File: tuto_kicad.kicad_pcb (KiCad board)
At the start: 4 copper layers, 48 x 38 mm, 46 parts, among them J201 Conn_ST_STDC14, J202 GPIO, J301 USB_C_Receptacle_USB2.0_16P, U201 STM32G431KBT6, U202 ADXL343, U301 MIC5317-3.3YM5-TR, U302 USBLC6-2SC6, Y201 16MHz

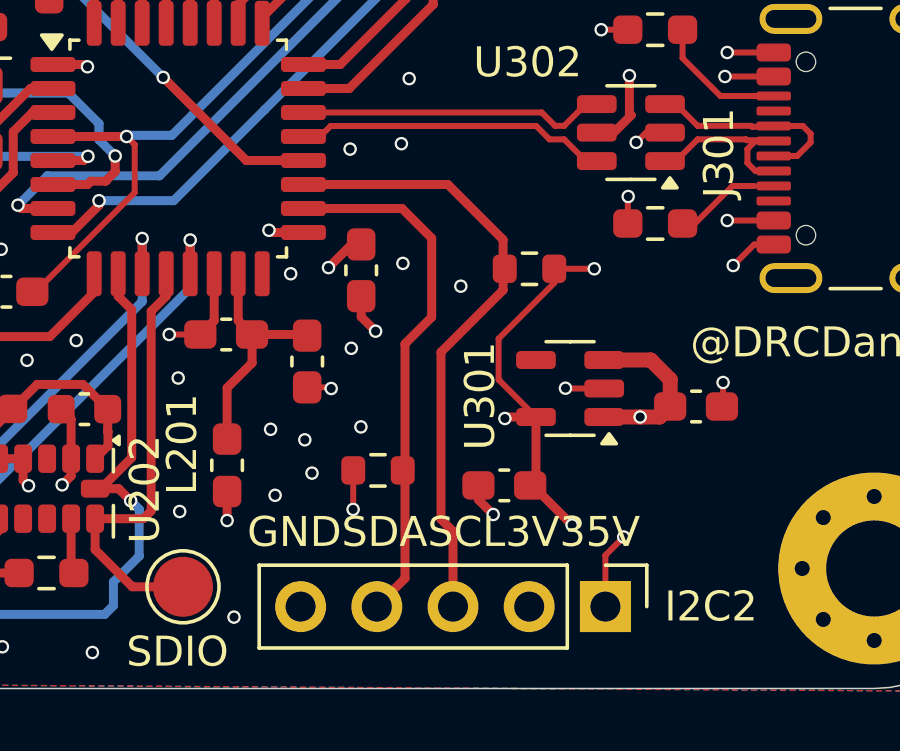
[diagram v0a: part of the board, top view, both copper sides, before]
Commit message: I2C2 SCL pull-up resistor moved
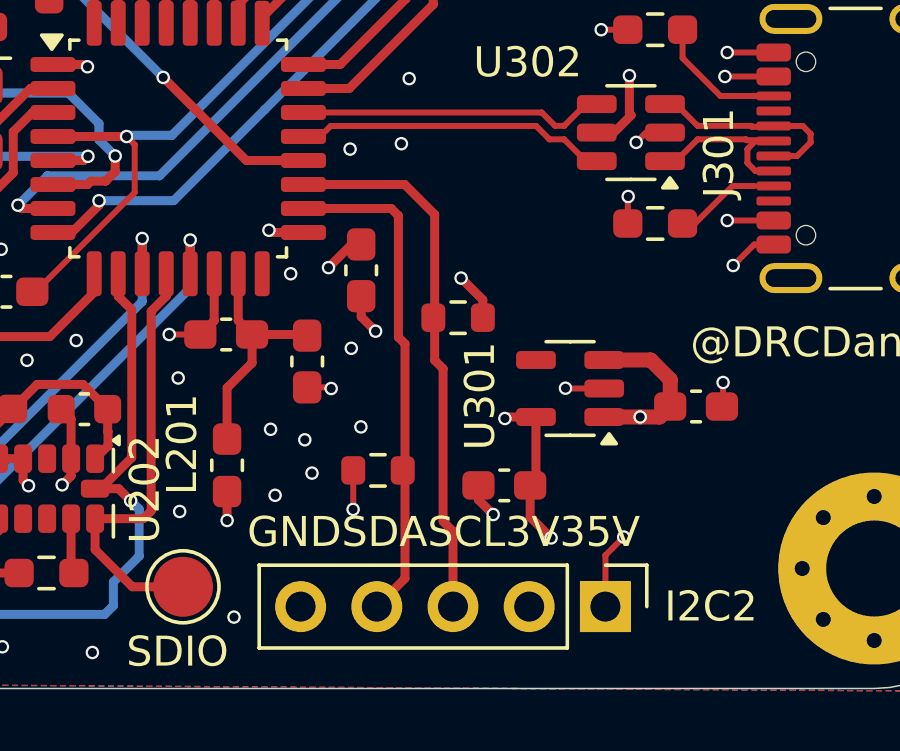
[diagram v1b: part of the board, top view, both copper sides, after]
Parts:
- moved R203 2.88 mm to (236.1, 91.6)
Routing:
- net +3.3V: track 24.6 -> 18.8 mm
- net I2C2_SCL: track 20.7 -> 18.1 mm
- net I2C2_SDA: track 17.7 -> 16.8 mm
- net GND: vias 115 -> 113
